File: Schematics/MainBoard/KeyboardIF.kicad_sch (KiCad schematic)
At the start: 7 parts, among them J14 KeyConn, U12 W65C51NxP, X2 1.8432MHz

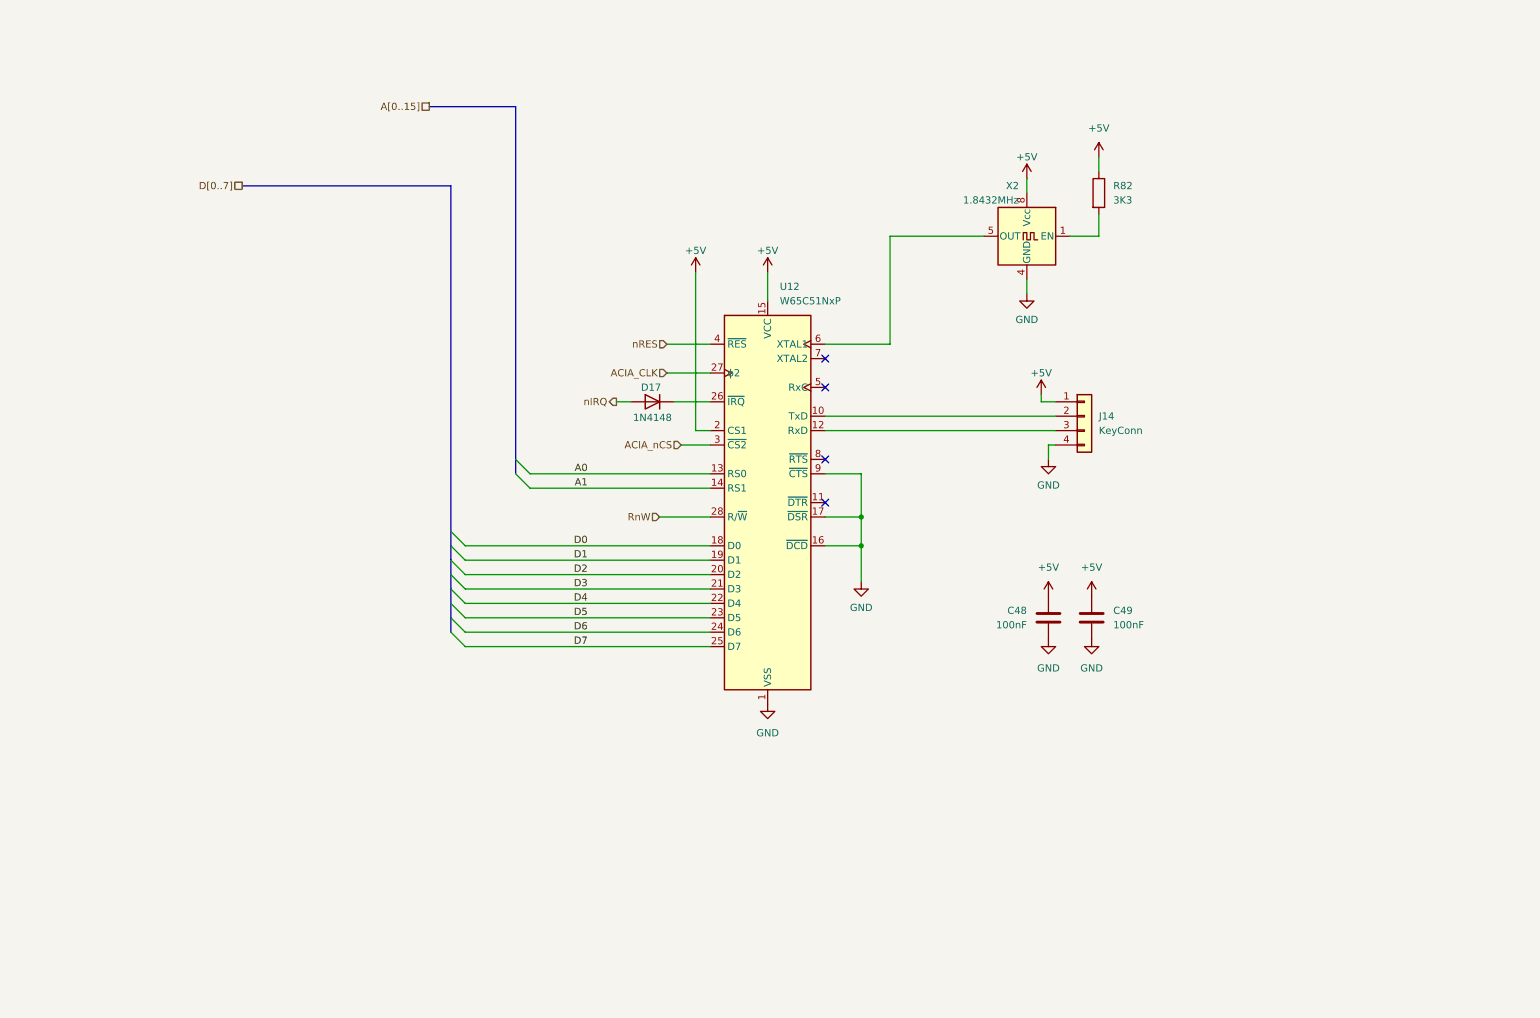
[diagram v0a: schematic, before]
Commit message: Move to a single board for everything (keyboard and main board)
Aim is to save height
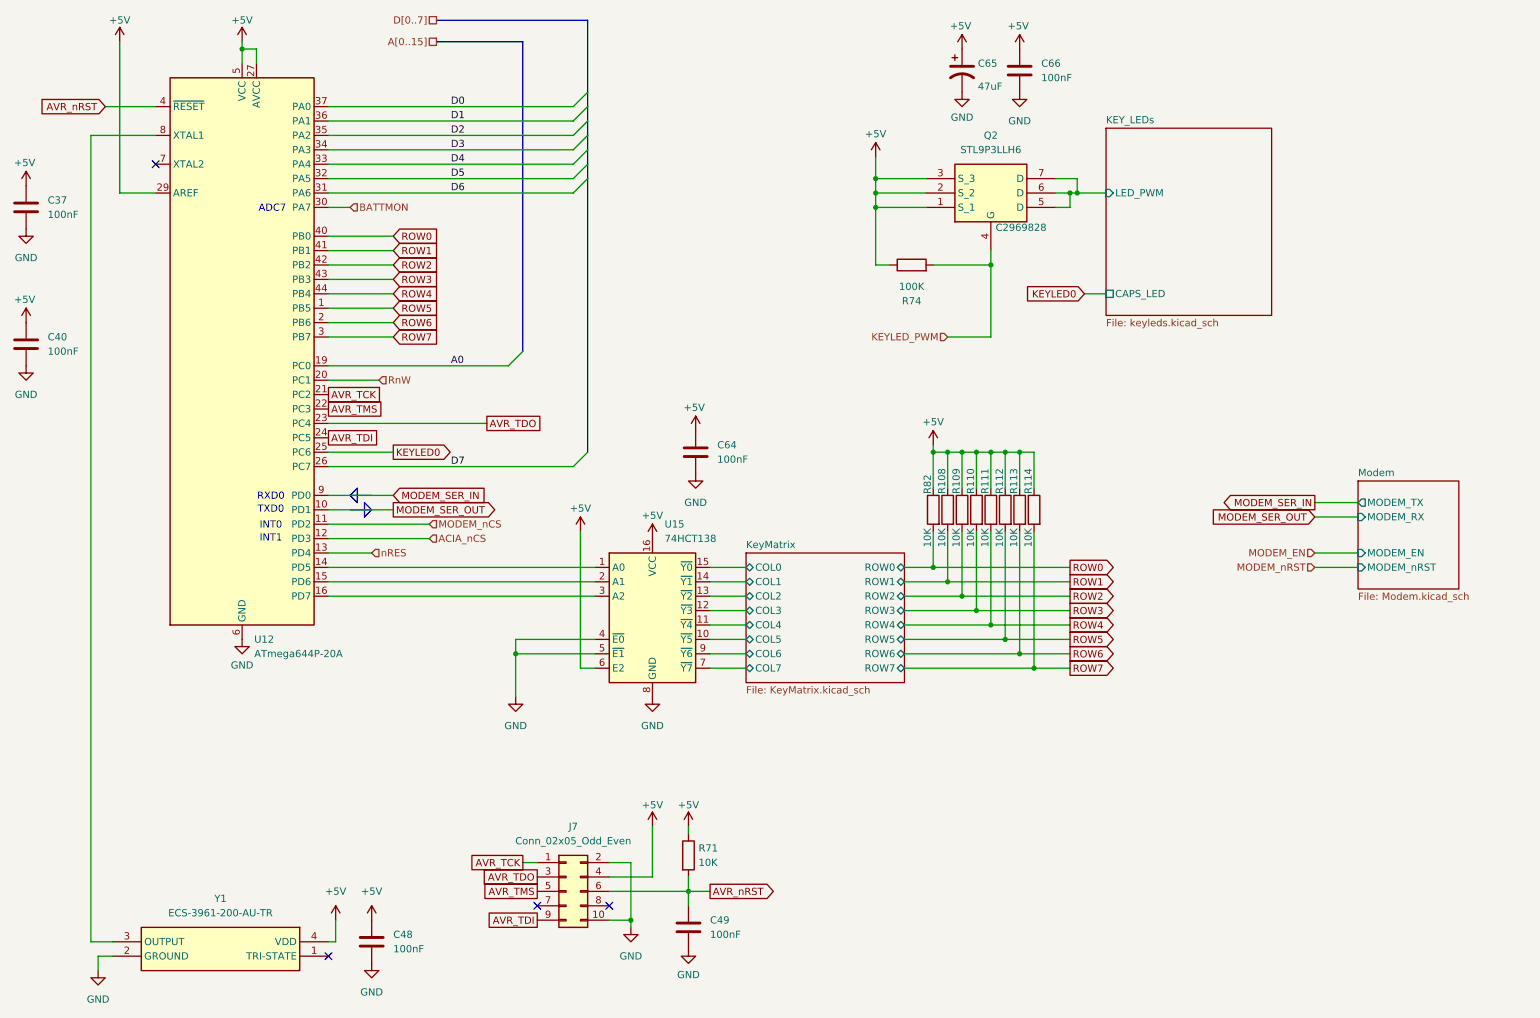
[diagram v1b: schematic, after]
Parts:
- removed D17: 1N4148, Diode_THT:D_DO-35_SOD27_P7.62mm_Horizontal, symbol Diode:1N4148
- removed J14: KeyConn, Connector_PinHeader_2.54mm:PinHeader_1x04_P2.54mm_Horizontal, symbol Connector_Generic:Conn_01x04
- removed U12: W65C51NxP, Package_DIP:DIP-28_W15.24mm, symbol 65xx-library:W65C51NxP
- removed X2: 1.8432MHz, Oscillator:Oscillator_DIP-8, symbol Oscillator:CXO_DIP8
- added C37, C40, C64, C66: 100nF, Capacitor_SMD:C_0805_2012Metric, symbol Device:C
- added C65: 47uF, Capacitor_SMD:C_1206_3216Metric, symbol Device:C_Polarized_US
- added J7: Conn_02x05_Odd_Even, Connector_PinHeader_2.54mm:PinHeader_2x05_P2.54mm_Horizontal, symbol Connector_Generic:Conn_02x05_Odd_Even
- added Q2: STL9P3LLH6, STL9P3LLH6:STL20N6F7, symbol STL9P3LLH6:STL9P3LLH6
- added R108, R109, R110, R111, R112, R113, R114, R71: 10K, Resistor_SMD:R_0603_1608Metric_Pad0.98x0.95mm_HandSolder, symbol Device:R
- added R74: 100K, Resistor_SMD:R_0402_1005Metric, symbol Device:R
- added U12: ATmega644P-20A, Package_QFP:TQFP-44_10x10mm_P0.8mm, symbol MCU_Microchip_ATmega:ATmega644P-20A
- added U15: 74HCT138, Package_SO:SSOP-16_5.3x6.2mm_P0.65mm, symbol 74xx:74HCT138
- added Y1: ECS-3961-200-AU-TR, ECS-3961-200-AU-TR:ECS3961200AUTR, symbol ECS-3961-200-AU-TR:ECS-3961-200-AU-TR
- C48: footprint Capacitor_SMD:C_0603_1608Metric -> Capacitor_SMD:C_0402_1005Metric
- C49: footprint Capacitor_SMD:C_0603_1608Metric -> Capacitor_SMD:C_0805_2012Metric; LCSC C113803 -> C49678
- R82: value 3K3 -> 10K; footprint Resistor_SMD:R_0402_1005Metric -> Resistor_SMD:R_0603_1608Metric_Pad0.98x0.95mm_HandSolder; LCSC C25890 -> DNF
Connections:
- net +5V: now also C37.1, C40.1, C64.1, C65.1, C66.1, J7.4 (Pin_4), Q2.1 (S_1), Q2.2 (S_2), Q2.3 (S_3), R108.1, R109.1, R110.1, R111.1, R112.1, R113.1, R114.1, R71.1, R74.1, U12.17 (VCC), U12.27 (AVCC), U12.29 (AREF), U12.38 (VCC), U12.5 (VCC), U15.16 (VCC), U15.6 (E2), Y1.4 (VDD); no longer C49.1
- net A0: now also U12.19 (PC0)
- net ACIA_nCS: now also U12.12 (PD3)
- net D0: now also U12.37 (PA0)
- net D1: now also U12.36 (PA1)
- net D2: now also U12.35 (PA2)
- net D3: now also U12.34 (PA3)
- net D4: now also U12.33 (PA4)
- net D5: now also U12.32 (PA5)
- net D6: now also U12.31 (PA6)
- net D7: now also U12.26 (PC7)
- net GND: now also C37.2, C40.2, C64.2, C65.2, C66.2, J7.10 (Pin_10), J7.2 (Pin_2), U12.18 (GND), U12.28 (GND), U12.39 (GND), U12.6 (GND), U15.4 (~{E0}), U15.5 (~{E1}), U15.8 (GND), Y1.2 (GROUND)
- net RnW: now also U12.20 (PC1)
- net nRES: now also U12.13 (PD4)
- net ROW0: now reaches R82.2
- net ROW0: now also U12.40 (PB0)
- new net: U12.14 (PD5), U15.1 (A0)
- new net: U12.15 (PD6), U15.2 (A1)
- new net: U12.16 (PD7), U15.3 (A2)
- new net: U12.8 (XTAL1), Y1.3 (OUTPUT)
- new net AVR_TCK: J7.1 (Pin_1), U12.21 (PC2)
- new net AVR_TDI: J7.9 (Pin_9), U12.24 (PC5)
- new net AVR_TDO: J7.3 (Pin_3), U12.23 (PC4)
- new net AVR_TMS: J7.5 (Pin_5), U12.22 (PC3)
- new net AVR_nRST: C49.1, J7.6 (Pin_6), R71.2, U12.4 (~{RESET})
- new net BATTMON: U12.30 (PA7)
- new net KEYLED0: U12.25 (PC6)
- new net KEYLED_PWM: Q2.4 (G), R74.2
- new net KEY_LEDs/LED_PWM: Q2.5 (D), Q2.6 (D), Q2.7 (D)
- new net KeyMatrix/COL0: U15.15 (~{Y0})
- new net KeyMatrix/COL1: U15.14 (~{Y1})
- new net KeyMatrix/COL2: U15.13 (~{Y2})
- new net KeyMatrix/COL3: U15.12 (~{Y3})
- new net KeyMatrix/COL4: U15.11 (~{Y4})
- new net KeyMatrix/COL5: U15.10 (~{Y5})
- new net KeyMatrix/COL6: U15.9 (~{Y6})
- new net KeyMatrix/COL7: U15.7 (~{Y7})
- new net MODEM_SER_IN: U12.9 (PD0)
- new net MODEM_SER_OUT: U12.10 (PD1)
- new net MODEM_nCS: U12.11 (PD2)
- new net ROW1: R108.2, U12.41 (PB1)
- new net ROW2: R109.2, U12.42 (PB2)
- new net ROW3: R110.2, U12.43 (PB3)
- new net ROW4: R111.2, U12.44 (PB4)
- new net ROW5: R112.2, U12.1 (PB5)
- new net ROW6: R113.2, U12.2 (PB6)
- new net ROW7: R114.2, U12.3 (PB7)
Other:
- added sheet KEY_LEDs (keyleds.kicad_sch)
- added sheet KeyMatrix (KeyMatrix.kicad_sch)
- added sheet Modem (Modem.kicad_sch)
- note added: "ADC7"
- note added: "INT0"
- note added: "INT1"
- note added: "RXD0"
- note added: "TXD0"

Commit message: Work on PCB
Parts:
- added C67, C68: 100nF, Capacitor_SMD:C_0402_1005Metric, symbol Device:C
- C37, C40, C49, C64, C66: footprint Capacitor_SMD:C_0805_2012Metric -> Capacitor_SMD:C_0402_1005Metric
- R108, R109, R110, R111, R112, R113, R114, R71, R82: footprint Resistor_SMD:R_0603_1608Metric_Pad0.98x0.95mm_HandSolder -> Resistor_SMD:R_0402_1005Metric
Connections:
- net +5V: now also C67.1, C68.1
- net GND: now also C67.2, C68.2

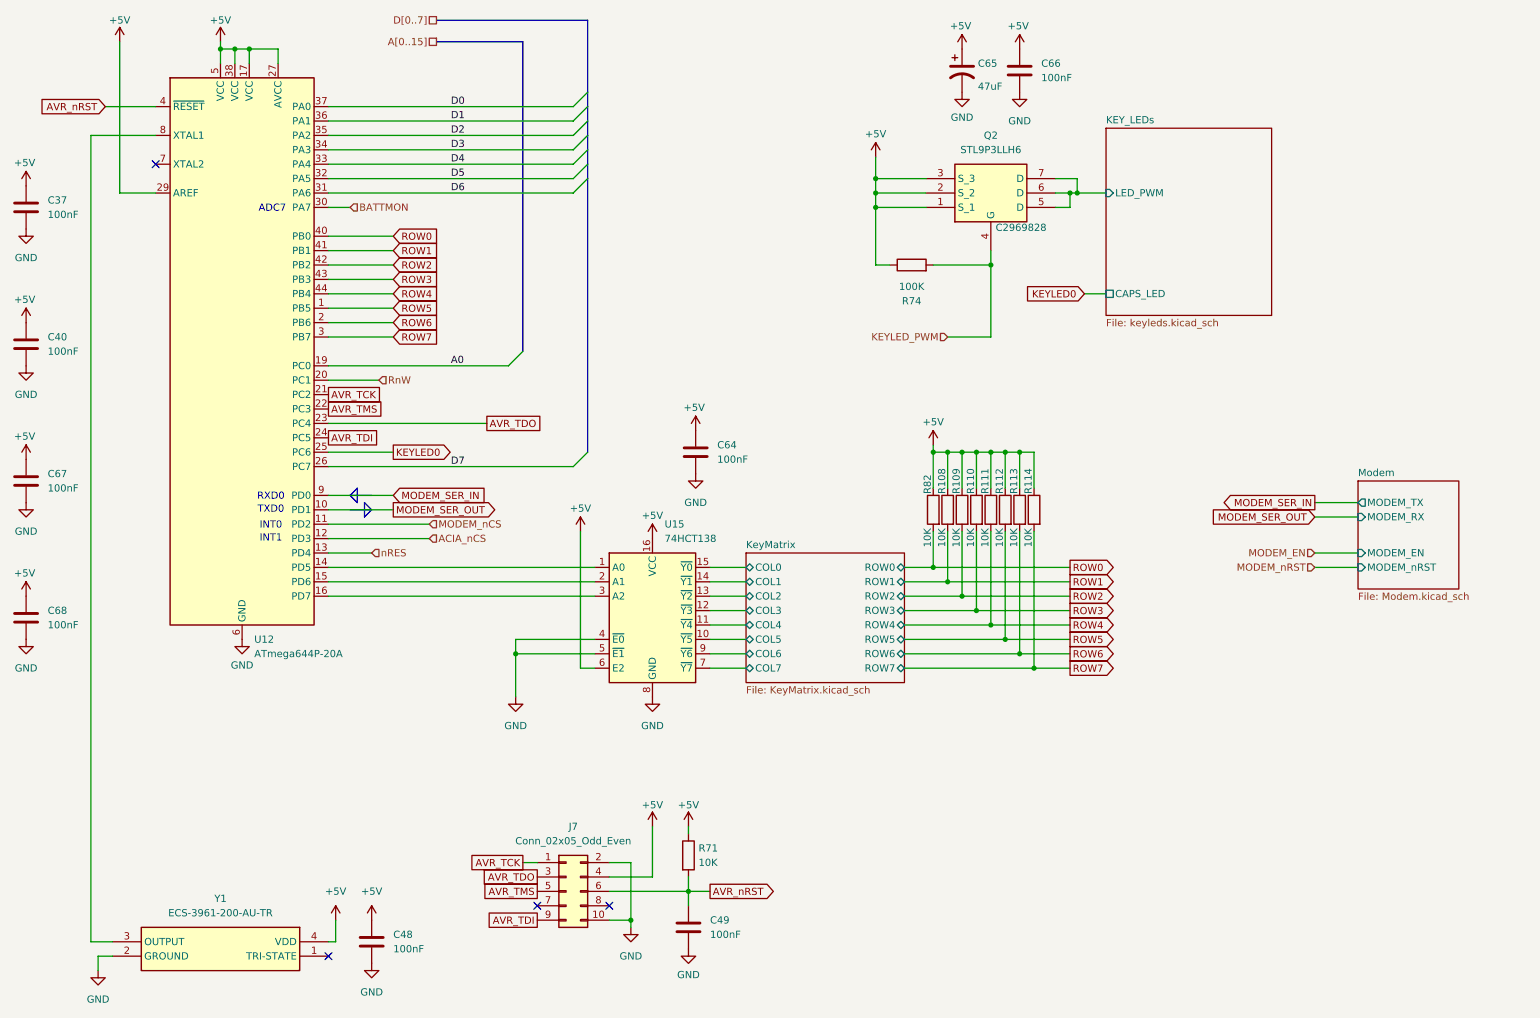
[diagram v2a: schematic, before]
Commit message: Work on PCB routing, added SwinSID
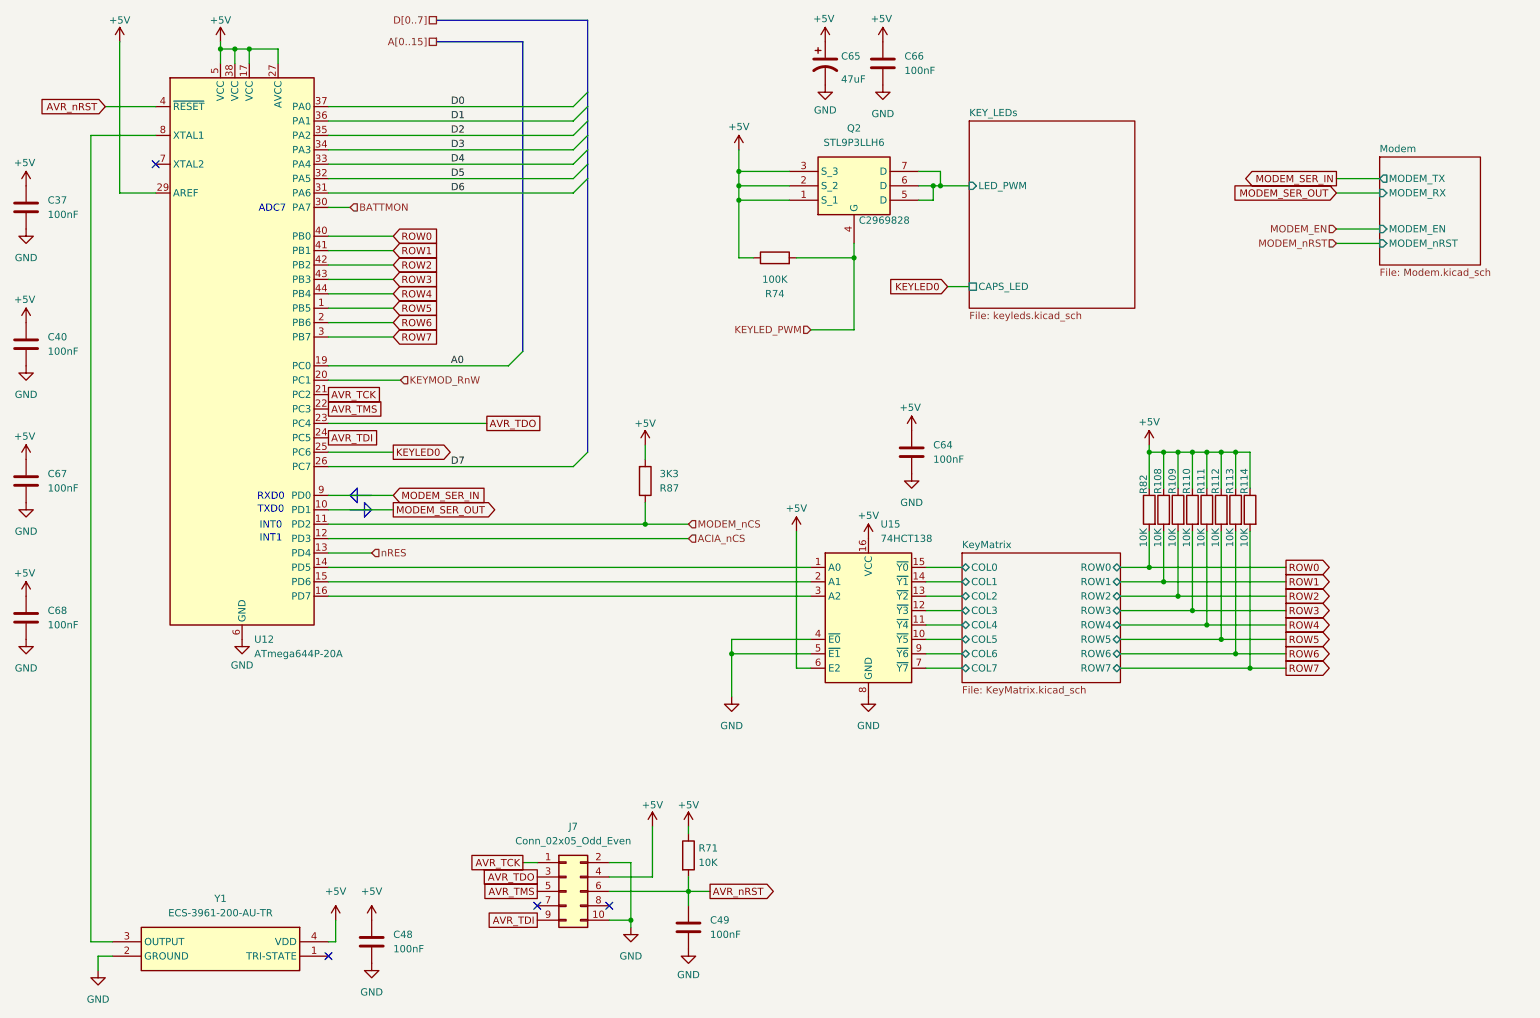
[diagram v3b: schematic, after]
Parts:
- added R87: 3K3, Resistor_SMD:R_0402_1005Metric, symbol Device:R
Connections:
- net +5V: now also R87.2
- net MODEM_nCS: now also R87.1
- net RnW renamed KEYMOD_RnW
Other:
- moved on the sheet: C64, C65, C66, Q2, R108, R109, R110, R111, R112, R113, R114, R74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

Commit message: Updates based on production files for JLC
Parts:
- C37, C40, C49, C64, C66, C67, C68: LCSC C49678 -> C307331
- C48: LCSC C113803 -> C307331
- J7: now not fitted
- R108, R109, R110, R111, R112, R113, R114, R71, R82: LCSC DNF -> C25744
- R74: LCSC DNF -> C25741
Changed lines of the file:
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@@
 			)
 		)
-		(property "LCSC" "C49678"
+		(property "LCSC" "C307331"
 			(at 17.78 102.87 0)
 			(effects
@@
 			)
 		)
-		(property "LCSC" "C49678"
+		(property "LCSC" "C307331"
 			(at 17.78 127 0)
 			(effects
@@
 			)
 		)
-		(property "LCSC" "C49678"
+		(property "LCSC" "C307331"
 			(at 17.78 78.74 0)
 			(effects
@@
 			)
 		)
-		(property "LCSC" "DNF"
+		(property "LCSC" "C25744"
 			(at 215.9 107.95 0)
 			(effects
@@
 			)
 		)
-		(property "LCSC" "DNF"
+		(property "LCSC" "C25744"
 			(at 233.68 107.95 0)
 			(effects
@@
 			)
 		)
-		(property "LCSC" "DNF"
+		(property "LCSC" "C25744"
 			(at 220.98 107.95 0)
 			(effects
@@
 			)
 		)
-		(property "LCSC" "DNF"
+		(property "LCSC" "C25744"
 			(at 226.06 107.95 0)
 			(effects
@@
 			)
 		)
-		(property "LCSC" "DNF"
+		(property "LCSC" "C25741"
 			(at 149.86 63.5 0)
 			(effects
@@
 			)
 		)
-		(property "LCSC" "C113803"
+		(property "LCSC" "C307331"
 			(at 78.74 184.15 0)
 			(effects
@@
 			)
 		)
-		(property "LCSC" "DNF"
+		(property "LCSC" "C25744"
 			(at 231.14 107.95 0)
 			(effects
@@
 			)
 		)
-		(property "LCSC" "C49678"
+		(property "LCSC" "C307331"
 			(at 134.62 181.61 0)
 			(effects
@@
 			)
 		)
-		(property "LCSC" "DNF"
+		(property "LCSC" "C25744"
 			(at 218.44 107.95 0)
 			(effects
@@
 		(in_bom yes)
 		(on_board yes)
-		(dnp no)
+		(dnp yes)
 		(property "Reference" "J7"
 			(at 114.3 163.83 0)
@@
 			)
 		)
-		(property "LCSC" "DNF"
+		(property "LCSC" "C25744"
 			(at 228.6 107.95 0)
 			(effects
@@
 			)
 		)
-		(property "LCSC" "DNF"
+		(property "LCSC" "C25744"
 			(at 223.52 107.95 0)
 			(effects
@@
 			)
 		)
-		(property "LCSC" "DNF"
+		(property "LCSC" "C25744"
 			(at 134.62 168.91 0)
 			(effects
@@
 			)
 		)
-		(property "LCSC" "C49678"
+		(property "LCSC" "C307331"
 			(at 168.91 29.21 0)
 			(effects
@@
 			)
 		)
-		(property "LCSC" "C49678"
+		(property "LCSC" "C307331"
 			(at 173.99 97.79 0)
 			(effects
@@
 			)
 		)
-		(property "LCSC" "C49678"
+		(property "LCSC" "C307331"
 			(at 17.78 54.61 0)
 			(effects
